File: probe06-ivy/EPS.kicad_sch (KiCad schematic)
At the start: 29 parts, among them J1 USB_B_Micro, SW2 xx, U2 MP1584EN, U3 AMS1117

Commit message: EPS design for 1 battery
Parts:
- removed C27, C29: 1uF, Capacitor_SMD:C_0805_2012Metric, symbol Device:C_Small
- removed C28, C30: 100nF, Capacitor_SMD:C_0805_2012Metric, symbol Device:C_Small
- removed D? (x2): D_Schottky, symbol Device:D_Schottky
- removed SW2: xx, Connector_JST:JST_EH_B2B-EH-A_1x02_P2.50mm_Vertical, symbol Connector_Generic:Conn_01x02
- removed U3: AMS1117, Package_TO_SOT_SMD:SOT-223-3_TabPin2, symbol Regulator_Linear:AMS1117
- added C? (x2): 22uF, symbol Device:C
- added D? (x2): D_Schottky, symbol Device:D_Schottky
- added D?: SS34, Diode_SMD:D_SMA, symbol Diode:SS34
- added L?: 22uH, symbol Device:L
- added R?: 2.2K, Resistor_SMD:R_0805_2012Metric, symbol Device:R
- added RV?: 100K, symbol Device:R_Potentiometer
- added U?: MT3608, Package_TO_SOT_SMD:SOT-23-6, symbol Regulator_Switching:MT3608
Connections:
- net +3V3: now also C24.1, C25.1, L2.2, RV1.2, RV1.3
- net +5V: now also C?.1, D?.1 (K), RV?.3; no longer C24.1, C25.1, L2.2, RV1.2, RV1.3
- net +5V_USB: now also D?.2 (A)
- net +BATT: now also C?.1, D?.2 (A), L?.1, U?.4 (EN), U?.5 (IN); no longer C20.1, C21.1, R7.1, U2.7 (VIN)
- net GND: now also C?.2, C?.2, R?.2, U?.2 (GND)
- new net: D?.2 (A), L?.2, U?.1 (SW)
- new net: R?.1, RV?.1
- new net: RV?.2, U?.3 (FB)
- new net 5V_USB: C20.1, C21.1, D?.1 (K), D?.1 (K), R7.1, U2.7 (VIN)
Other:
- note added: "3.3 V Buck Converter"
- note added: "5 V Boost Converter"
- note removed: "3V3 Regulator"
- note removed: "Buck Converter"
- moved on the sheet: BATT?, BT1, C20, C21, C22, C23, C24, C25, C26, D1, J1, L2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

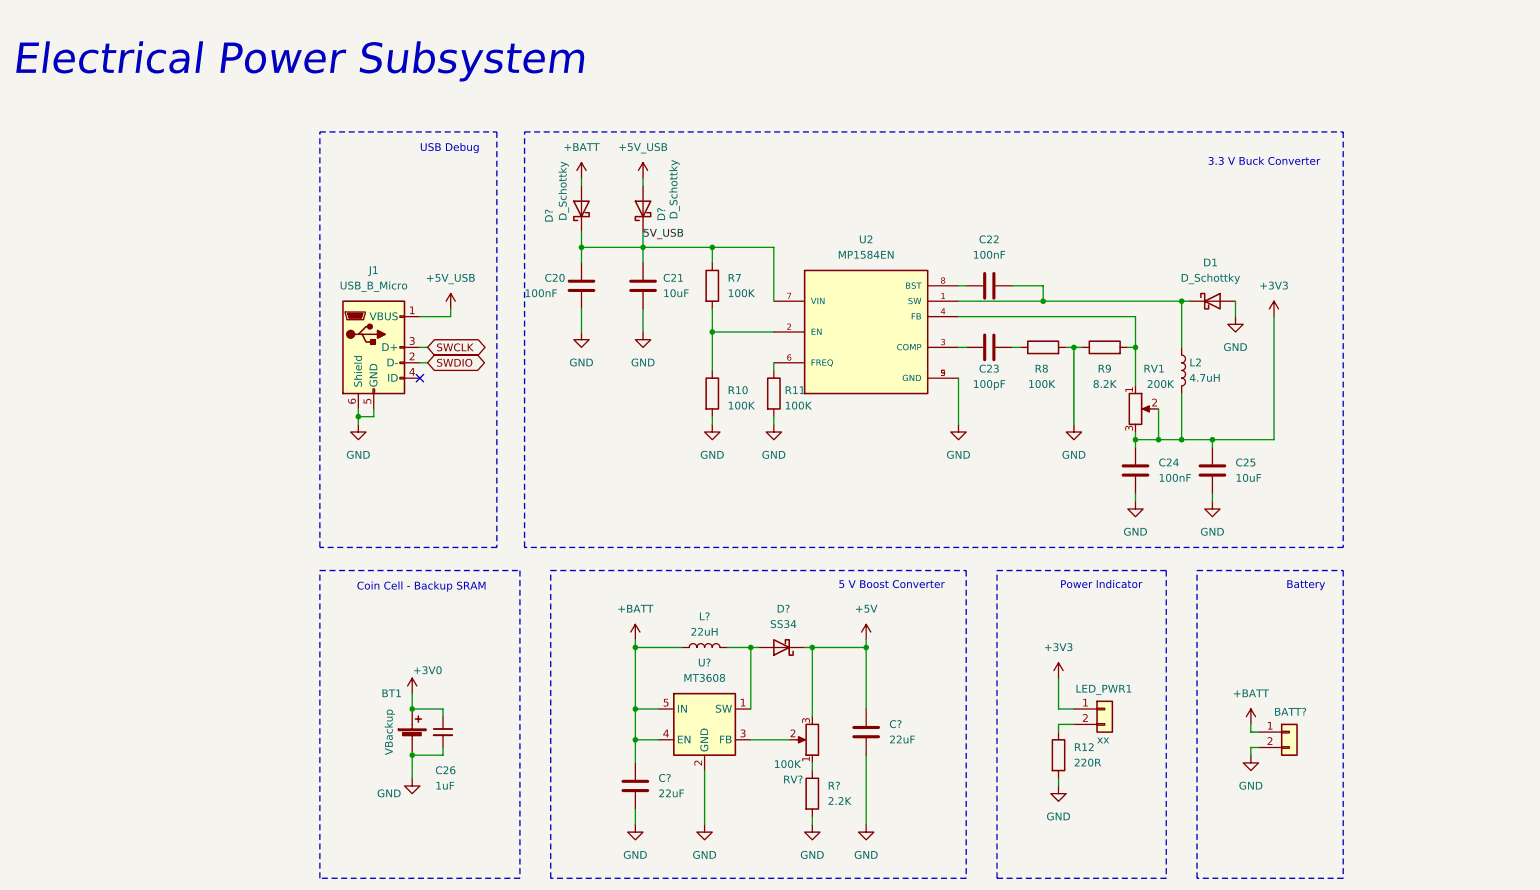
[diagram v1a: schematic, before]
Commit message: Routing Layout - add footprint to all components - pcb shape and dimension - component placement
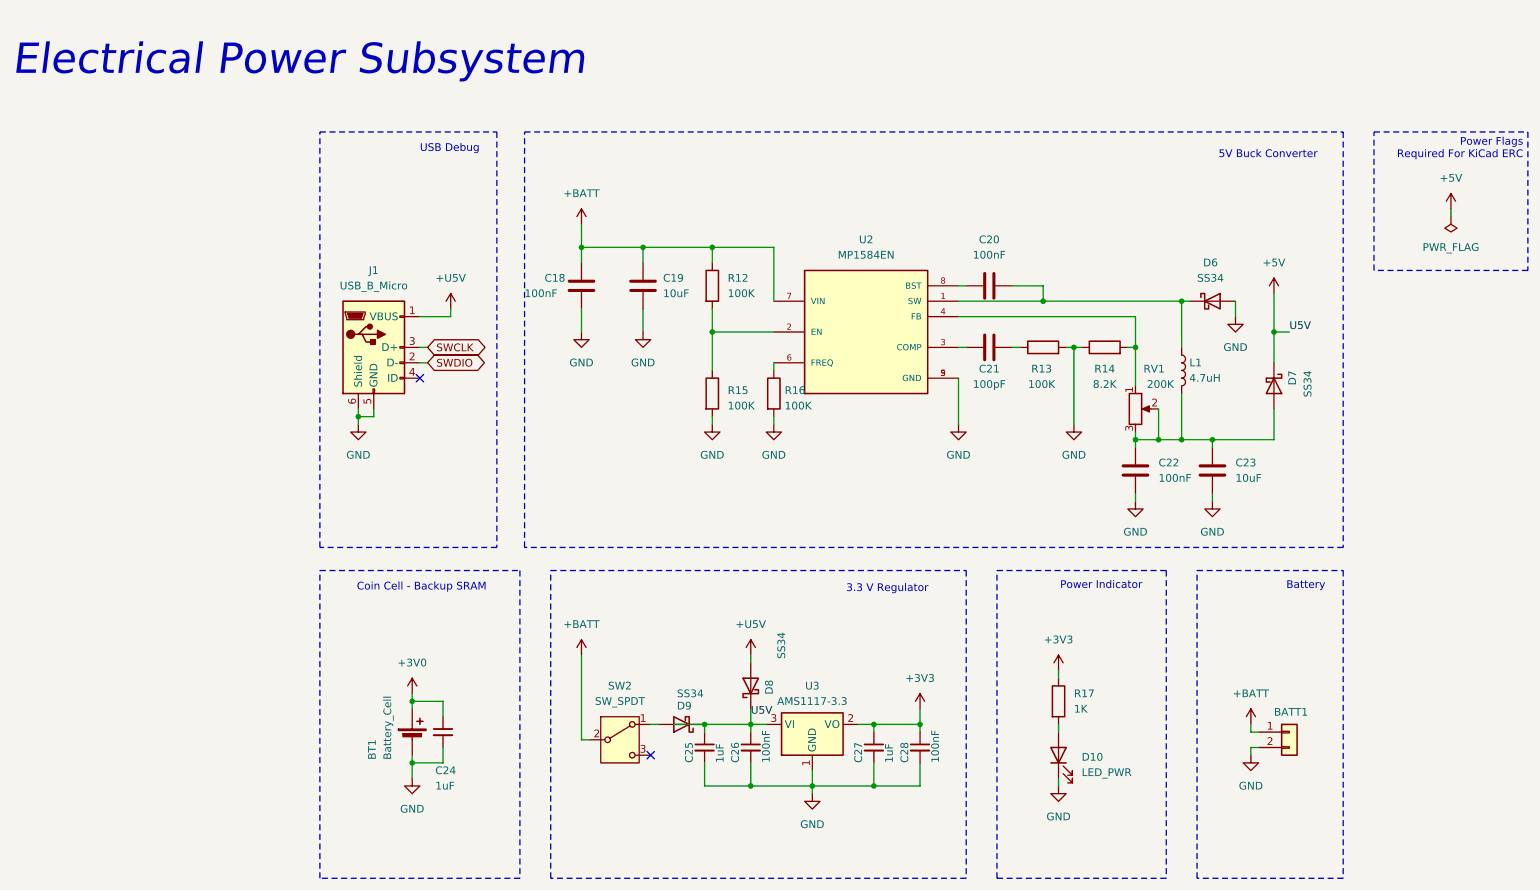
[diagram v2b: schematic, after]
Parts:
- removed C? (x2): 22uF, symbol Device:C
- removed D? (x2): D_Schottky, symbol Device:D_Schottky
- removed D?: SS34, Diode_SMD:D_SMA, symbol Diode:SS34
- removed L?: 22uH, symbol Device:L
- removed LED_PWR1: xx, Connector_JST:JST_EH_B2B-EH-A_1x02_P2.50mm_Vertical, symbol Connector_Generic:Conn_01x02
- removed R?: 2.2K, Resistor_SMD:R_0805_2012Metric, symbol Device:R
- removed RV?: 100K, symbol Device:R_Potentiometer
- removed U?: MT3608, Package_TO_SOT_SMD:SOT-23-6, symbol Regulator_Switching:MT3608
- added C25, C27: 1uF, Capacitor_SMD:C_0805_2012Metric, symbol Device:C_Small
- added C26, C28: 100nF, Capacitor_SMD:C_0805_2012Metric, symbol Device:C_Small
- added D10: LED_PWR, LED_SMD:LED_0805_2012Metric, symbol Device:LED
- added D7, D8, D9: SS34, Diode_SMD:D_SMA, symbol Device:D_Schottky
- added SW2: SW_SPDT, Button_Switch_THT:SW_Slide_SPDT_Angled_CK_OS102011MA1Q, symbol Switch:SW_SPDT
- added U3: AMS1117-3.3, Package_TO_SOT_SMD:SOT-223-3_TabPin2, symbol Regulator_Linear:AMS1117-3.3
- BATT1: renamed from BATT?; footprint Connector_JST:JST_EH_B2B-EH-A_1x02_P2.50mm_Vertical -> Connector_PinHeader_2.54mm:PinHeader_1x02_P2.54mm_Vertical
- BT1: value VBackup -> Battery_Cell; footprint Battery:BatteryHolder_ComfortableElectronic_CH273-2450_1x2450 -> digikey-footprints:Battery_Holder_Coin_2032_BS-7
- C18: renamed from C20; footprint (none) -> Capacitor_SMD:C_0603_1608Metric
- C19: renamed from C21; footprint (none) -> Capacitor_SMD:C_0805_2012Metric
- C20: renamed from C22; footprint (none) -> Capacitor_SMD:C_0603_1608Metric
- C21: renamed from C23; footprint (none) -> Capacitor_SMD:C_0603_1608Metric
- C22: renamed from C24; footprint (none) -> Capacitor_SMD:C_0603_1608Metric
- C23: renamed from C25; footprint (none) -> Capacitor_SMD:C_0805_2012Metric
- D6: renamed from D1; value D_Schottky -> SS34; footprint (none) -> Diode_SMD:D_SMA
- L1: renamed from L2; footprint (none) -> Inductor_SMD:L_6.3x6.3_H3
- R12: renamed from R7; footprint (none) -> Resistor_SMD:R_0603_1608Metric
- R13: renamed from R8; footprint (none) -> Resistor_SMD:R_0603_1608Metric
- R14: renamed from R9; footprint (none) -> Resistor_SMD:R_0603_1608Metric
- R15: renamed from R10; footprint (none) -> Resistor_SMD:R_0603_1608Metric
- R16: renamed from R11; footprint (none) -> Resistor_SMD:R_0603_1608Metric
- R17: renamed from R12; value 220R -> 1K
- RV1: footprint (none) -> TC33X-2-103E:TRIM_TC33X-2-103E
- renumbered C26 to C24
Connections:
- net 5V_USB is gone; now on net +BATT: C18.1, C19.1, R12.1, U2.7 (VIN)
- net +3V3: now also R17.1, C27.1, C28.1, U3.2 (VO); no longer C22.1, C23.1, L1.2, RV1.2, RV1.3
- net +5V: now also C25.1, C26.1, D7.1 (K), D8.1 (K), D9.1 (K), U3.3 (VI)
- net +BATT: now also SW2.2 (B)
- net GND: now also C25.2, C26.2, C27.2, C28.2, D10.1 (K), U3.1 (GND); no longer R17.2
- net +5V_USB renamed +U5V
- net +U5V: now also D8.2 (A)
- new net: D10.2 (A), R17.2
- new net: C22.1, C23.1, D7.2 (A), L1.2, RV1.2, RV1.3
- new net: D9.2 (A), SW2.1 (A)
- no-connect marks 1 -> 2
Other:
- note added: "3.3 V Regulator"
- note added: "5V Buck Converter"
- note added: "Power Flags Required For KiCad ERC"
- note removed: "3.3 V Buck Converter"
- note removed: "5 V Boost Converter"
- title: CanSat Avionics -> CanSat Avionics - Auto Gyro Descender
- moved on the sheet: R17
